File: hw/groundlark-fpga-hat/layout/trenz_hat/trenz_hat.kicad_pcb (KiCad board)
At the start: 2 copper layers, 195 parts

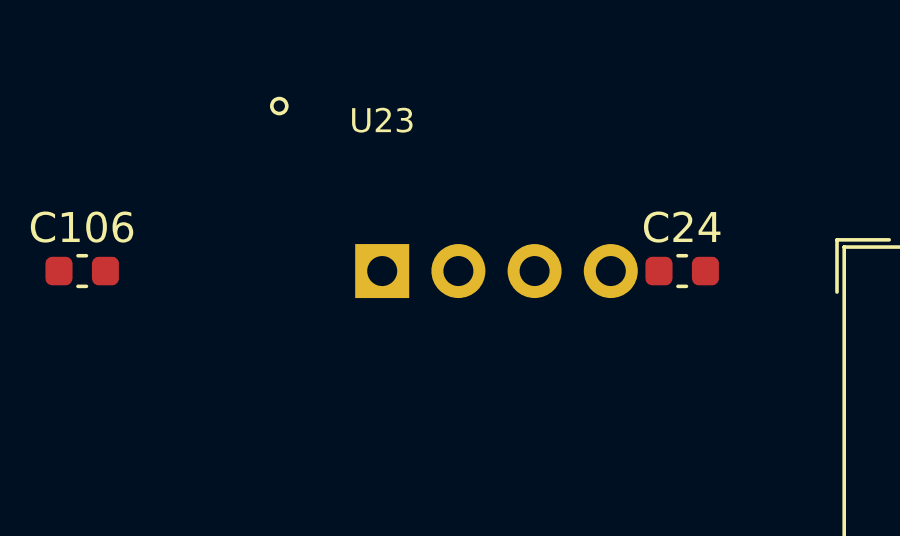
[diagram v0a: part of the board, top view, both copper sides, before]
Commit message: Update DAQHAT pressure sensor and assembly sourcing
Replace D90 with TPD2E2U06QDCKRQ1 and redesign U23 around SDP32-125PA. Synchronize routed CAD, native SES, models, supplier records, acquisition drivers, contracts, simulations, tests and documentation.

Record dated stock checks for 71 catalog identities and preserve the release gate for 52 unverified supplier placements. Generated manufacturing packages remain local and ignored.

Validation: repository structure and diff checks pass; prior full lab run passed 25 of 26 stages, with 301 software tests and 221 of 222 hardware tests passing. The remaining hardware test blocks unverified placements. Browser interaction and physical qualification remain pending.
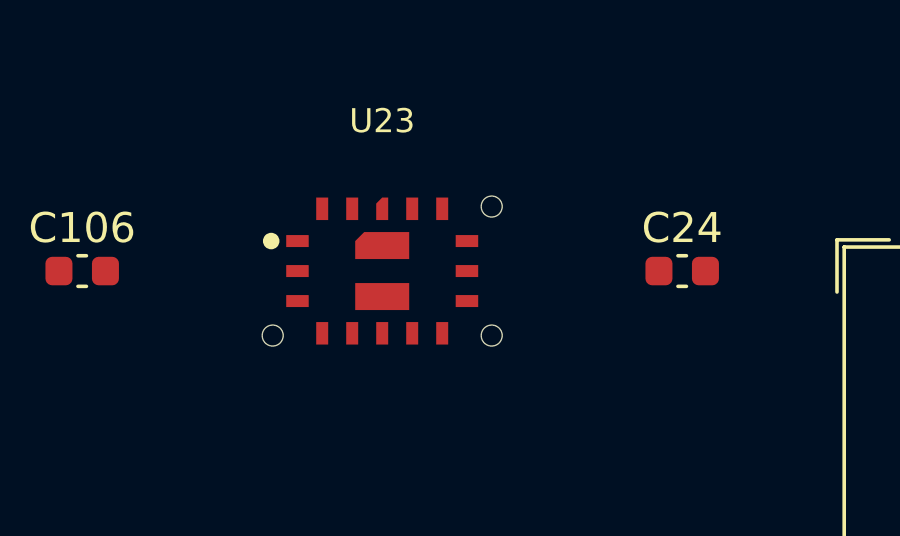
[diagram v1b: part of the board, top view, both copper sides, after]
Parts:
- U23: footprint elec:Groundlark__DLVR_E1BS -> elec:Groundlark__SDP32
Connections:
- U23 pad 2: SENS_3V3 -> GND
- U23 pad 3: I2C_SDA -> GND
- U23 pad 4: I2C_SCL -> PRESSURE_NC_4
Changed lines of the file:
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@@
 	(net 257 "GNSS_LDO")
 	(net 258 "GNSS_BIAS")
-	(net 361 "I2C_SDA")
-	(net 362 "I2C_SCL")
 	(net 363 "PI_I2C_SCL")
 	(net 364 "PI_I2C_SDA")
 	(net 278 "GNSS_FAULT_NC")
+	(net 279 "PRESSURE_NC_12")
+	(net 311 "PRESSURE_NC_13")
+	(net 346 "PRESSURE_NC_14")
+	(net 347 "PRESSURE_NC_15")
+	(net 350 "PRESSURE_NC_16")
+	(net 365 "I2C_SDA")
+	(net 361 "I2C_SCL")
+	(net 366 "PRESSURE_NC_4")
 	(footprint "elec:Connector_PinHeader_2.54mm__PinHeader_2x20_P2.54mm_Vertical"
 		(layer "F.Cu")
@@
 			(size 1.475 0.4)
 			(layers "F.Cu" "F.Mask" "F.Paste")
-			(net 361 "I2C_SDA")
+			(net 365 "I2C_SDA")
 			(roundrect_rratio 0.25)
 		)
@@
 			(size 1.475 0.4)
 			(layers "F.Cu" "F.Mask" "F.Paste")
-			(net 362 "I2C_SCL")
+			(net 361 "I2C_SCL")
 			(roundrect_rratio 0.25)
 		)
@@
 			(size 1.95 0.6)
 			(layers "F.Cu" "F.Mask" "F.Paste")
-			(net 361 "I2C_SDA")
+			(net 365 "I2C_SDA")
 			(roundrect_rratio 0.25)
 		)
@@
 			(size 1.95 0.6)
 			(layers "F.Cu" "F.Mask" "F.Paste")
-			(net 362 "I2C_SCL")
+			(net 361 "I2C_SCL")
 			(roundrect_rratio 0.25)
 		)
@@
 			(size 0.8 0.95)
 			(layers "F.Cu" "F.Mask" "F.Paste")
-			(net 361 "I2C_SDA")
+			(net 365 "I2C_SDA")
 			(roundrect_rratio 0.25)
 		)
@@
 			(size 0.8 0.95)
 			(layers "F.Cu" "F.Mask" "F.Paste")
-			(net 362 "I2C_SCL")
+			(net 361 "I2C_SCL")
 			(roundrect_rratio 0.25)
 		)
@@
 		)
 	)
-	(footprint "elec:Groundlark__DLVR_E1BS"
+	(footprint "elec:Groundlark__SDP32"
 		(layer "F.Cu")
 		(at 1180 0 0)
@@
 			(hide yes)
 		)
+		(attr smd)
 		(fp_circle
-			(center -3.43 -5.5)
-			(end -3.18 -5.5)
+			(center -3.7 -1)
+			(end -3.5 -1)
 			(stroke
-				(width 0.12)
-				(type solid)
+				(width 0.15)
+				(type default)
 			)
-			(fill no)
+			(fill yes)
 			(layer "F.SilkS")
 		)
 		(fp_rect
-			(start -3.03 -5.8)
-			(end 10.3 -0.5)
+			(start -4.5 -3)
+			(end 4.5 3)
 			(stroke
 				(width 0.05)
-				(type solid)
+				(type default)
 			)
 			(fill no)
@@
 		)
 		(fp_rect
-			(start -2.73 -5.5)
-			(end 10 -0.8)
+			(start -4.25 -2.75)
+			(end 4.25 2.75)
 			(stroke
 				(width 0.1)
-				(type solid)
+				(type default)
 			)
 			(fill no)
 			(layer "F.Fab")
 		)
-		(pad "1" thru_hole rect
-			(at 0 0)
-			(size 1.8 1.8)
-			(drill 1)
+		(pad "" np_thru_hole circle
+			(at -3.65 2.15)
+			(size 0.7 0.7)
+			(drill 0.7)
 			(layers "*.Cu" "*.Mask")
-			(remove_unused_layers no)
-			(net 141 "GND")
 		)
-		(pad "2" thru_hole oval
-			(at 2.54 0)
-			(size 1.8 1.8)
-			(drill 1)
-			(layers "*.Cu" "*.Mask")
-			(remove_unused_layers no)
-			(net 1 "SENS_3V3")
+		(pad "" smd roundrect
+			(at 0 -0.85)
+			(size 1.6 0.7)
+			(layers "F.Paste")
+			(roundrect_rratio 0.25)
+			(chamfer_ratio 0.4285714)
+			(chamfer top_left)
+		)
+		(pad "" smd rect
+			(at 0 0.85)
+			(size 1.6 0.7)
+			(layers "F.Paste")
 		)
-		(pad "3" thru_hole oval
-			(at 5.08 0)
-			(size 1.8 1.8)
-			(drill 1)
+		(pad "" np_thru_hole circle
+			(at 3.65 -2.15)
+			(size 0.7 0.7)
+			(drill 0.7)
 			(layers "*.Cu" "*.Mask")
-			(remove_unused_layers no)
-			(net 361 "I2C_SDA")
 		)
-		(pad "4" thru_hole oval
-			(at 7.62 0)
-			(size 1.8 1.8)
-			(drill 1)
+		(pad "" np_thru_hole circle
+			(at 3.65 2.15)
+			(size 0.7 0.7)
+			(drill 0.7)
 			(layers "*.Cu" "*.Mask")
-			(remove_unused_layers no)
-			(net 362 "I2C_SCL")
+		)
+		(pad "1" smd rect
+			(at -2.825 -1)
+			(size 0.75 0.4)
+			(layers "F.Cu" "F.Mask" "F.Paste")
+			(net 141 "GND")
+		)
+		(pad "2" smd rect
+			(at -2.825 0)
+			(size 0.75 0.4)
+			(layers "F.Cu" "F.Mask" "F.Paste")
+			(net 141 "GND")
+		)
+		(pad "3" smd rect
+			(at -2.825 1)
+			(size 0.75 0.4)
+			(layers "F.Cu" "F.Mask" "F.Paste")
+			(net 141 "GND")
+		)
+		(pad "4" smd rect
+			(at -2 2.075)
+			(size 0.4 0.75)
+			(layers "F.Cu" "F.Mask" "F.Paste")
+			(net 366 "PRESSURE_NC_4")
+		)
+		(pad "5" smd rect
+			(at -1 2.075)
+			(size 0.4 0.75)
+			(layers "F.Cu" "F.Mask" "F.Paste")
+			(net 361 "I2C_SCL")
+		)
+		(pad "6" smd rect
+			(at 0 2.075)
+			(size 0.4 0.75)
+			(layers "F.Cu" "F.Mask" "F.Paste")
+			(net 141 "GND")
+		)
+		(pad "7" smd rect
+			(at 1 2.075)
+			(size 0.4 0.75)
+			(layers "F.Cu" "F.Mask" "F.Paste")
+			(net 1 "SENS_3V3")
+		)
+		(pad "8" smd rect
+			(at 2 2.075)
+			(size 0.4 0.75)
+			(layers "F.Cu" "F.Mask" "F.Paste")
+			(net 365 "I2C_SDA")
+		)
+		(pad "9" smd rect
+			(at 2.825 1)
+			(size 0.75 0.4)
+			(layers "F.Cu" "F.Mask" "F.Paste")
+			(net 141 "GND")
+		)
+		(pad "10" smd rect
+			(at 2.825 0)
+			(size 0.75 0.4)
+			(layers "F.Cu" "F.Mask" "F.Paste")
+			(net 141 "GND")
+		)
+		(pad "11" smd rect
+			(at 2.825 -1)
+			(size 0.75 0.4)
+			(layers "F.Cu" "F.Mask" "F.Paste")
+			(net 141 "GND")
+		)
+		(pad "12" smd rect
+			(at 2 -2.075)
+			(size 0.4 0.75)
+			(layers "F.Cu" "F.Mask" "F.Paste")
+			(net 279 "PRESSURE_NC_12")
+		)
+		(pad "13" smd rect
+			(at 1 -2.075)
+			(size 0.4 0.75)
+			(layers "F.Cu" "F.Mask" "F.Paste")
+			(net 311 "PRESSURE_NC_13")
+		)
+		(pad "14" smd roundrect
+			(at 0 -2.075)
+			(size 0.4 0.75)
+			(layers "F.Cu" "F.Mask" "F.Paste")
+			(net 346 "PRESSURE_NC_14")
+			(roundrect_rratio 0.25)
+			(chamfer_ratio 0.5)
+			(chamfer top_left)
+		)
+		(pad "15" smd rect
+			(at -1 -2.075)
+			(size 0.4 0.75)
+			(layers "F.Cu" "F.Mask" "F.Paste")
+			(net 347 "PRESSURE_NC_15")
+		)
+		(pad "16" smd rect
+			(at -2 -2.075)
+			(size 0.4 0.75)
+			(layers "F.Cu" "F.Mask" "F.Paste")
+			(net 350 "PRESSURE_NC_16")
+		)
+		(pad "17" smd roundrect
+			(at 0 -0.85)
+			(size 1.8 0.9)
+			(layers "F.Cu" "F.Mask")
+			(net 141 "GND")
+			(roundrect_rratio 0.25)
+			(chamfer_ratio 0.3333333)
+			(chamfer top_left)
+		)
+		(pad "17" smd rect
+			(at 0 0.85)
+			(size 1.8 0.9)
+			(layers "F.Cu" "F.Mask")
+			(net 141 "GND")
 		)
 		(embedded_fonts no)

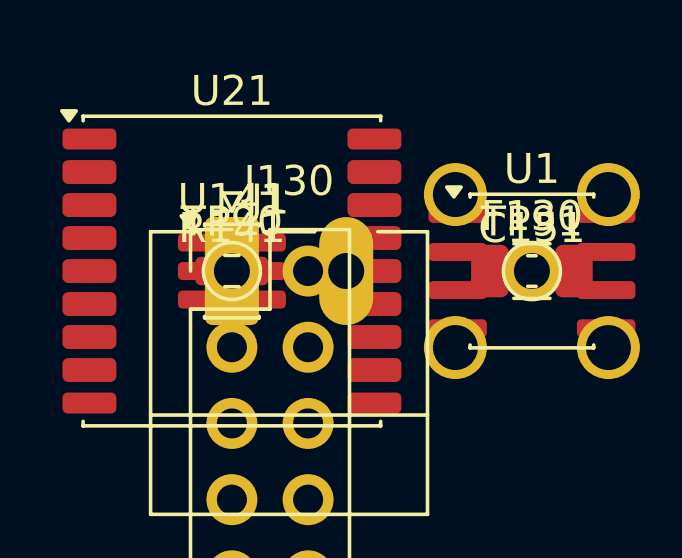
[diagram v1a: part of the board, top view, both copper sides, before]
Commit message: Strengthen DAQHAT power copper and validate native layout
Extend Pi supply pours to J1, add output via arrays and an FPGA distribution
bridge, spread D130 heat, correct GNSS RF width, and add UART idle bias.
Synchronize circuit, native CAD, schematic, SES, models and assembly mapping.

Extract native DC resistance, screen adjacent-layer coupling, preserve checks
under Python optimization, and disable I2C/I3C on the shared SPI IMUs.
Refresh specifications, supplier identity records and validation evidence.

Native ERC/DRC, route replay, simulations and 302 software tests pass. The final
hardware run passes 234/235; 52 supplier placement holds still prevent release.
All 71 exact catalog identities passed a fresh public inventory check.
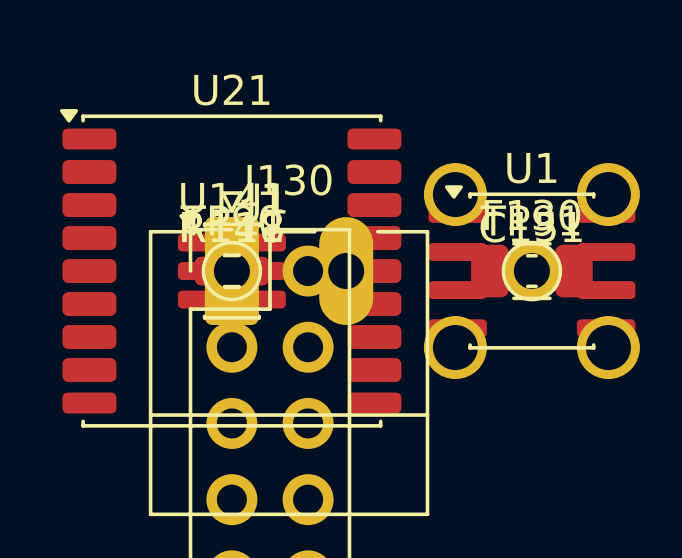
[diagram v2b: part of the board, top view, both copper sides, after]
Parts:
- added R118: , elec:Resistor_SMD__R_0603_1608Metric, F.Cu at (0.00, 0.00)
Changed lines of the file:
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@@
 	(net 292 "PI_GEO_DRDY_N")
 	(net 293 "u42-9")
-	(net 294 "PI_UART_RX")
 	(net 295 "PI_UART_TX")
 	(net 296 "FPGA_UART_DRIVE")
@@
 	(net 361 "I2C_SCL")
 	(net 366 "PRESSURE_NC_4")
+	(net 294 "PI_UART_RX")
 	(footprint "elec:Connector_PinHeader_2.54mm__PinHeader_2x20_P2.54mm_Vertical"
 		(layer "F.Cu")
@@
 			(offset
 				(xyz 0 0 0)
+			)
+			(scale
+				(xyz 1 1 1)
+			)
+			(rotate
+				(xyz 0 0 0)
+			)
+		)
+	)
+	(footprint "elec:Resistor_SMD__R_0603_1608Metric"
+		(layer "F.Cu")
+		(at 0 0 0)
+		(descr "Resistor SMD 0603 (1608 Metric), square (rectangular) end terminal, IPC-7351 nominal, (Body size source: IPC-SM-782 page 72, https://www.pcb-3d.com/wordpress/wp-content/uploads/ipc-sm-782a_amendment_1_and_2.pdf), generated with kicad-footprint-generator")
+		(tags "resistor")
+		(property "Reference" "R118"
+			(at 0 -1.43 0)
+			(layer "F.SilkS")
+			(effects
+				(font
+					(size 1 1)
+					(thickness 0.15)
+				)
+			)
+		)
+		(property "Value" ""
+			(at 0 1.43 0)
+			(layer "F.Fab")
+			(effects
+				(font
+					(size 1 1)
+					(thickness 0.15)
+				)
+			)
+		)
+		(property "atopile_address" "r118"
+			(at 0 0 0)
+			(layer "User.9")
+			(hide yes)
+		)
+		(attr smd)
+		(fp_line
+			(start -0.237258 -0.5225)
+			(end 0.237258 -0.5225)
+			(stroke
+				(width 0.12)
+				(type solid)
+			)
+			(layer "F.SilkS")
+		)
+		(fp_line
+			(start -0.237258 0.5225)
+			(end 0.237258 0.5225)
+			(stroke
+				(width 0.12)
+				(type solid)
+			)
+			(layer "F.SilkS")
+		)
+		(fp_rect
+			(start -1.48 -0.73)
+			(end 1.48 0.73)
+			(stroke
+				(width 0.05)
+				(type solid)
+			)
+			(fill no)
+			(layer "F.CrtYd")
+		)
+		(fp_rect
+			(start -0.8 -0.4125)
+			(end 0.8 0.4125)
+			(stroke
+				(width 0.1)
+				(type solid)
+			)
+			(fill no)
+			(layer "F.Fab")
+		)
+		(pad "1" smd roundrect
+			(at -0.825 0)
+			(size 0.8 0.95)
+			(layers "F.Cu" "F.Mask" "F.Paste")
+			(net 294 "PI_UART_RX")
+			(roundrect_rratio 0.25)
+		)
+		(pad "2" smd roundrect
+			(at 0.825 0)
+			(size 0.8 0.95)
+			(layers "F.Cu" "F.Mask" "F.Paste")
+			(net 3 "PI_3V3")
+			(roundrect_rratio 0.25)
+		)
+		(embedded_fonts no)
+		(model "${KICAD9_3DMODEL_DIR}/Resistor_SMD.3dshapes/R_0603_1608Metric.step"
+			(offset
+				(xyz 0 0 0)

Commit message: Fix GNSS RF margin and broaden pressure filter robustness
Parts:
- added L141: , elec:GNSS_HP0402, F.Cu at (0.00, 0.00)
- L140: footprint elec:GNSS_L0402 -> elec:GNSS_HP0402
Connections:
- C148 pad 2: GNSS_RF -> GNSS_MATCH
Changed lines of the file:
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@@
 	(net 348 "u140-3")
 	(net 349 "u140-4")
-	(net 351 "GNSS_RF")
 	(net 352 "u21-13")
 	(net 353 "u21-14")
@@
 	(net 366 "PRESSURE_NC_4")
 	(net 294 "PI_UART_RX")
+	(net 362 "GNSS_RF")
+	(net 351 "GNSS_MATCH")
 	(footprint "elec:Connector_PinHeader_2.54mm__PinHeader_2x20_P2.54mm_Vertical"
 		(layer "F.Cu")
@@
 			(size 1.8 0.8)
 			(layers "F.Cu" "F.Mask" "F.Paste")
-			(net 351 "GNSS_RF")
+			(net 362 "GNSS_RF")
 			(roundrect_rratio 0.25)
 		)
@@
 			(size 0.56 0.62)
 			(layers "F.Cu" "F.Paste" "F.Mask")
-			(net 351 "GNSS_RF")
+			(net 351 "GNSS_MATCH")
 			(roundrect_rratio 0.2)
 		)
 	)
-	(footprint "elec:GNSS_L0402"
+	(footprint "elec:GNSS_HP0402"
 		(layer "F.Cu")
 		(at 50 0 0)
@@
 		(attr smd)
 		(fp_rect
-			(start -0.8 -0.5)
-			(end 0.8 0.5)
+			(start -0.83 -0.61)
+			(end 0.83 0.61)
 			(stroke
 				(width 0.05)
@@
 		)
 		(fp_rect
-			(start -0.5 -0.25)
-			(end 0.5 0.25)
+			(start -0.572 -0.355)
+			(end 0.572 0.355)
 			(stroke
 				(width 0.05)
@@
 		)
 	)
+	(footprint "elec:GNSS_HP0402"
+		(layer "F.Cu")
+		(at 0 0 0)
+		(descr "Coilcraft 0402HP; enlarged 0.56 x 0.62 mm lands, 0.96 mm centers. Body max 1.17 x 0.71 x 0.82 mm including solder. Doc 526-1.")
+		(property "Reference" "L141"
+			(at 0 -1.2)
+			(layer "F.Fab")
+			(effects
+				(font
+					(size 0.6 0.6)
+					(thickness 0.1)
+				)
+			)
+		)
+		(property "Value" ""
+			(at 0 1.2)
+			(layer "F.Fab")
+			(effects
+				(font
+					(size 0.6 0.6)
+					(thickness 0.1)
+				)
+			)
+		)
+		(property "atopile_address" "l141"
+			(at 0 0 0)
+			(layer "User.9")
+			(hide yes)
+		)
+		(attr smd)
+		(fp_rect
+			(start -0.83 -0.61)
+			(end 0.83 0.61)
+			(stroke
+				(width 0.05)
+				(type default)
+			)
+			(fill none)
+			(layer "F.CrtYd")
+		)
+		(fp_rect
+			(start -0.572 -0.355)
+			(end 0.572 0.355)
+			(stroke
+				(width 0.05)
+				(type default)
+			)
+			(fill none)
+			(layer "F.Fab")
+		)
+		(pad "1" smd roundrect
+			(at -0.48 0)
+			(size 0.56 0.62)
+			(layers "F.Cu" "F.Paste" "F.Mask")
+			(net 351 "GNSS_MATCH")
+			(roundrect_rratio 0.2)
+		)
+		(pad "2" smd roundrect
+			(at 0.48 0)
+			(size 0.56 0.62)
+			(layers "F.Cu" "F.Paste" "F.Mask")
+			(net 362 "GNSS_RF")
+			(roundrect_rratio 0.2)
+		)
+	)
